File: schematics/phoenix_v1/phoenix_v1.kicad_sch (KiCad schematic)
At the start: 1 part, among them U1 ESP32-DevKitC

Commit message: v1 schematic
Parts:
- removed U1: ESP32-DevKitC, PCM_Espressif:ESP32-DevKitC, symbol PCM_Espressif:ESP32-DevKitC
- added D1, D2, D3: LED, symbol Device:LED
- added L1: L, symbol Device:L
- added R1, R2, R3: R, symbol Device:R
- added R4, R5: 4.7k, symbol Device:R
- added SW2: RotaryEncoder_Switch, symbol Device:RotaryEncoder_Switch
- added U2: MAX31856, Package_SO:TSSOP-14_4.4x5mm_P0.65mm, symbol Sensor_Temperature:MAX31856
- added U3: NHD-C0220BIZ, Display:NHD-C0220BiZ, symbol Display_Character:NHD-C0220BIZ
- added U4: HHG1D-1, Relay_THT:Relay_NCR_HHG1D-1, symbol Relay_SolidState:HHG1D-1
- added U5: ESP32-S3-DevKitC, PCM_Espressif:ESP32-S3-DevKitC, symbol PCM_Espressif:ESP32-S3-DevKitC
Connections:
- new net: R1.1, U5.14 (GPIO46)
- new net: R2.1, U5.28 (GPIO47)
- new net: R3.1, U5.29 (GPIO48)
- new net: D3.2 (A), R3.2
- new net: D1.2 (A), R1.2
- new net: D2.2 (A), R2.2
- new net: L1.1, U4.1
- new net +3.3V: R4.1, R5.1, U5.1 (3V3), U5.2 (3V3)
- new net +5V: U2.5 (AVDD), U2.8 (DVDD), U3.5 (VDD), U5.21 (5V)
- new net AC: L1.2, U4.2
- new net ENC_A: SW2.A, U5.33 (GPIO36)
- new net ENC_B: SW2.B, U5.34 (GPIO37)
- new net ENC_SW: SW2.S2, U5.35 (GPIO38)
- new net GND: D1.1 (K), D2.1 (K), D3.1 (K), SW2.C, SW2.S1, U2.1 (AGND), U2.14 (DGND), U3.4 (VSS), U4.4, U5.22 (GND), U5.23 (GND), U5.24 (GND), U5.44 (GND)
- new net SCL: R4.2, U3.2 (SCL), U5.13 (GPIO3/ADC1_CH2)
- new net SDA: R5.2, U3.3 (SDA), U5.40 (GPIO2/ADC1_CH1)
- new net SSR_PWM: U4.3, U5.27 (GPIO21)
- new net THERMO_CS: U2.9 (~{CS}), U5.16 (GPIO10/ADC1_CH9)
- new net THERMO_SCK: U2.10 (SCK), U5.18 (GPIO12/ADC2_CH1)
- new net THERMO_SDI: U2.12 (SDI), U5.17 (GPIO11/ADC2_CH0)
- new net THERMO_SDO: U2.11 (SDO), U5.19 (GPIO13/ADC2_CH2)
- no-connect marks 0 -> 10

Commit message: screw terminal
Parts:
- added J1: Screw_Terminal_01x02, symbol Connector:Screw_Terminal_01x02
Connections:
- net GND: now also J1.1 (Pin_1)
- net SSR_PWM: now also J1.2 (Pin_2)
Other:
- moved on the sheet: L1, U4

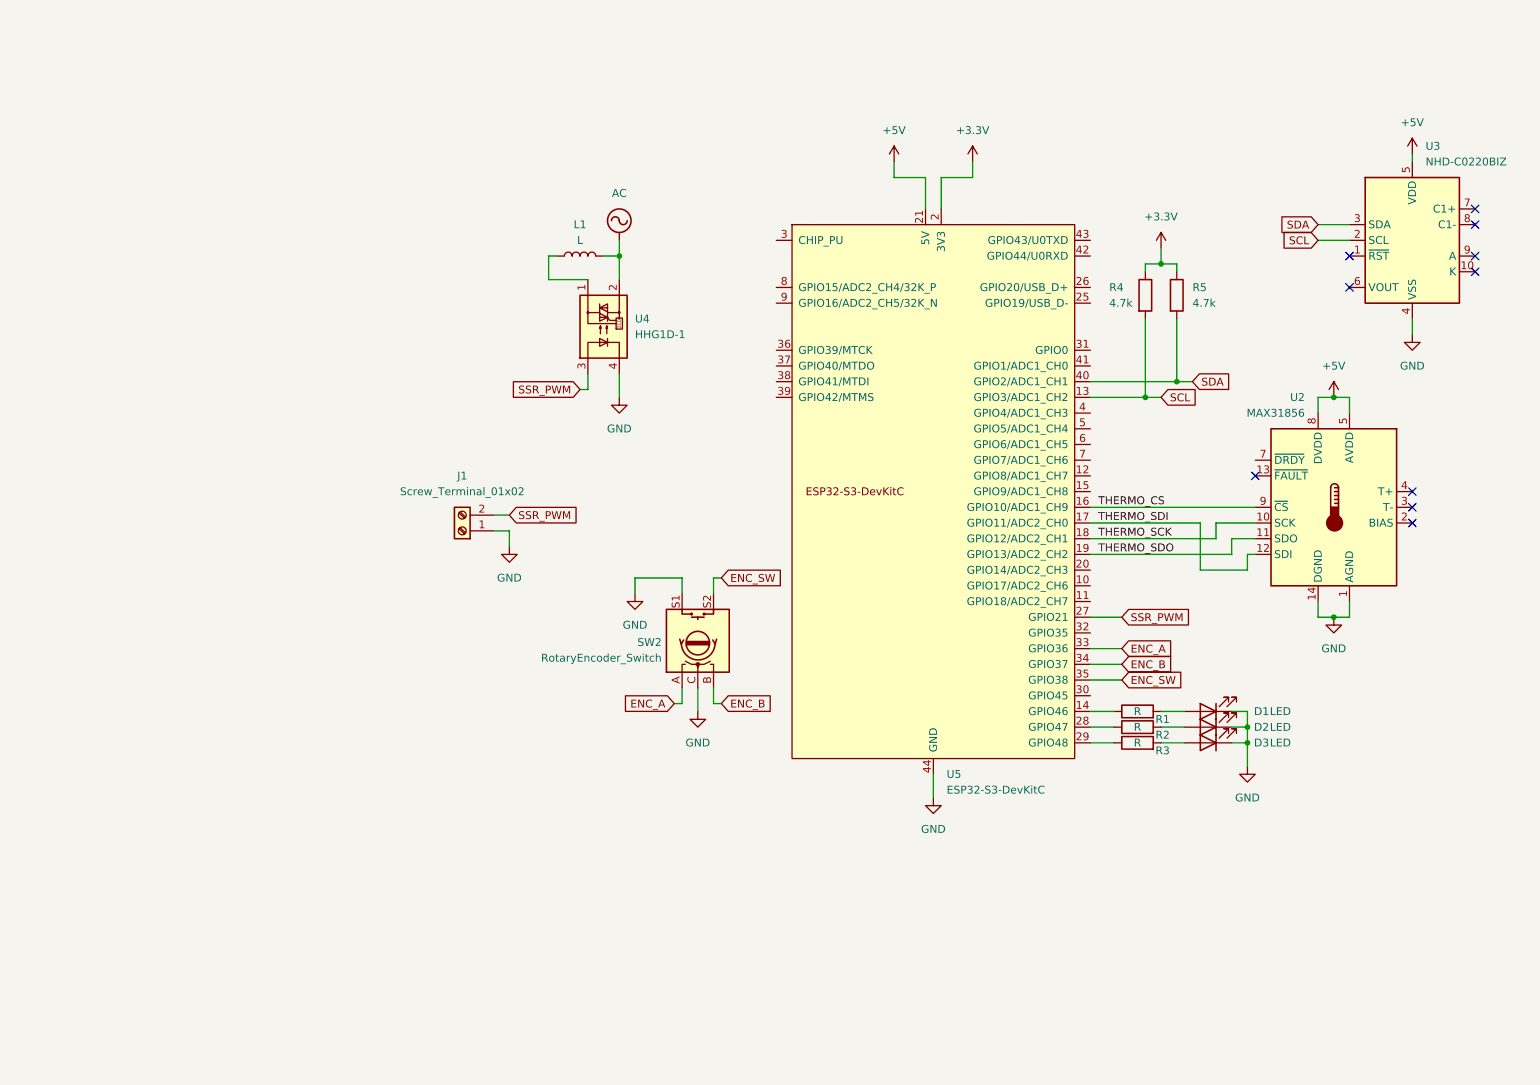
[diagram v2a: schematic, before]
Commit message: assign footprints (#17)
* layout

* fix duplicate

* max31856 socket

* add ncs

* upload screw terminal files

* footprint assignment

* upload MAX31856 eagle-converted source

* create custom footprint for MAX31856 header

* upload pec stuff

* use project footprint library

* extract PEC footprint and sym

* finish assigning footprints and update PCB

---------

Co-authored-by: Waterloo Hacker Fab <waterloofab@hackerfabmacmini.uwaterloo.ca>
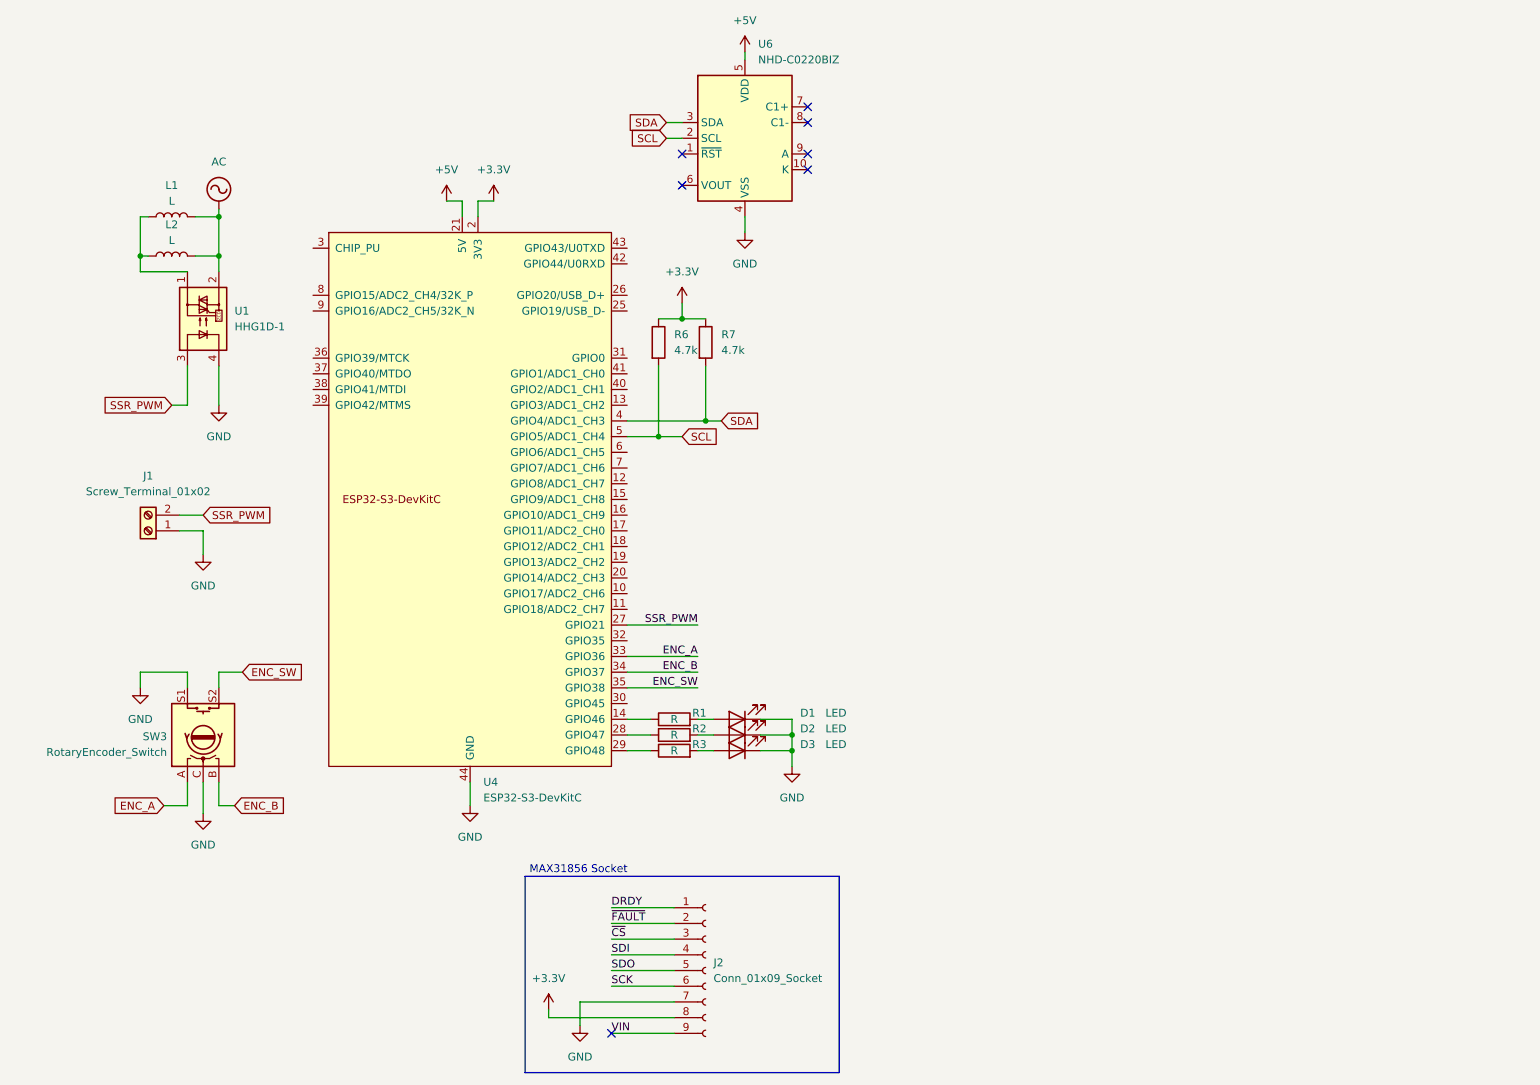
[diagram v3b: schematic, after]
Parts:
- removed R4, R5: 4.7k, symbol Device:R
- removed SW2: RotaryEncoder_Switch, symbol Device:RotaryEncoder_Switch
- removed U2: MAX31856, Package_SO:TSSOP-14_4.4x5mm_P0.65mm, symbol Sensor_Temperature:MAX31856
- removed U3: NHD-C0220BIZ, Display:NHD-C0220BiZ, symbol Display_Character:NHD-C0220BIZ
- removed U4: HHG1D-1, Relay_THT:Relay_NCR_HHG1D-1, symbol Relay_SolidState:HHG1D-1
- removed U5: ESP32-S3-DevKitC, PCM_Espressif:ESP32-S3-DevKitC, symbol PCM_Espressif:ESP32-S3-DevKitC
- added J2: Conn_01x09_Socket, !footprints:MAX31856_HEADER, symbol Connector:Conn_01x09_Socket
- added L2: L, symbol Device:L
- added R6, R7: 4.7k, Resistor_SMD:R_0805_2012Metric_Pad1.20x1.40mm_HandSolder, symbol Device:R
- added SW3: RotaryEncoder_Switch, !footprints:PEC164120FS0012, symbol Device:RotaryEncoder_Switch
- added U1: HHG1D-1, Relay_THT:Relay_NCR_HHG1D-1, symbol Relay_SolidState:HHG1D-1
- added U4: ESP32-S3-DevKitC, PCM_Espressif:ESP32-S3-DevKitC, symbol PCM_Espressif:ESP32-S3-DevKitC
- added U6: NHD-C0220BIZ, Display:NHD-C0220BiZ, symbol Display_Character:NHD-C0220BIZ
- D1, D2, D3: footprint (none) -> Diode_SMD:D_0805_2012Metric_Pad1.15x1.40mm_HandSolder
- J1: footprint (none) -> phoenix_footprints:TE_282837-2
- R1, R2, R3: footprint (none) -> Resistor_SMD:R_0805_2012Metric_Pad1.20x1.40mm_HandSolder
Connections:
- net +3.3V: now also J2.8 (Pin_8), R6.1, R7.1, U4.1 (3V3), U4.2 (3V3)
- net +5V: now also U4.21 (5V), U6.5 (VDD)
- net AC: now also L2.2, U1.2
- net ENC_A: now also SW3.A, U4.33 (GPIO36)
- net ENC_B: now also SW3.B, U4.34 (GPIO37)
- net ENC_SW: now also SW3.S2, U4.35 (GPIO38)
- net GND: now also J2.7 (Pin_7), SW3.C, SW3.S1, U1.4, U4.22 (GND), U4.23 (GND), U4.24 (GND), U4.44 (GND), U6.4 (VSS)
- net SCL: now also R6.2, U4.5 (GPIO5/ADC1_CH4), U6.2 (SCL)
- net SDA: now also R7.2, U4.4 (GPIO4/ADC1_CH3), U6.3 (SDA)
- net SSR_PWM: now also U1.3, U4.27 (GPIO21)
- net at R1.1: now also U4.14 (GPIO46)
- net at R2.1: now also U4.28 (GPIO47)
- net at R3.1: now also U4.29 (GPIO48)
- net at L1.1: now also L2.1, U1.1
- new net DRDY: J2.1 (Pin_1)
- new net SCK: J2.6 (Pin_6)
- new net SDI: J2.4 (Pin_4)
- new net SDO: J2.5 (Pin_5)
- new net VIN: J2.9 (Pin_9)
- new net ~{CS}: J2.3 (Pin_3)
- new net ~{FAULT}: J2.2 (Pin_2)
- no-connect marks 10 -> 7
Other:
- note added: "MAX31856 Socket"

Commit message: exclude relay and inductors from board
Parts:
- U1: footprint Relay_THT:Relay_NCR_HHG1D-1 -> (none)
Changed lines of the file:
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@@
 		(exclude_from_sim no)
 		(in_bom yes)
-		(on_board yes)
+		(on_board no)
 		(dnp no)
 		(fields_autoplaced yes)
@@
 		(exclude_from_sim no)
 		(in_bom yes)
-		(on_board yes)
+		(on_board no)
 		(dnp no)
 		(fields_autoplaced yes)
@@
 			)
 		)
-		(property "Footprint" "Relay_THT:Relay_NCR_HHG1D-1"
+		(property "Footprint" ""
 			(at 55.88 67.31 0)
 			(effects
@@
 		(exclude_from_sim no)
 		(in_bom yes)
-		(on_board yes)
-		(dnp no)
-		(fields_autoplaced yes)
+		(on_board no)
+		(dnp no)
+		(fields_autoplaced yes)

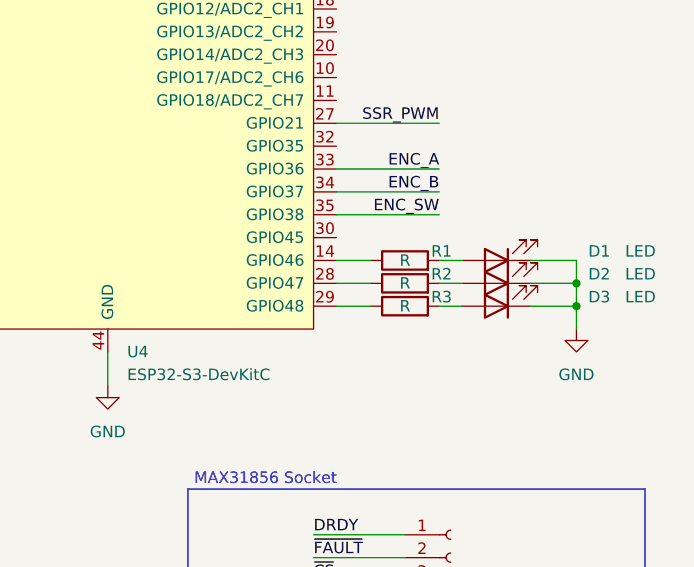
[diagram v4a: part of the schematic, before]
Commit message: set R for leds
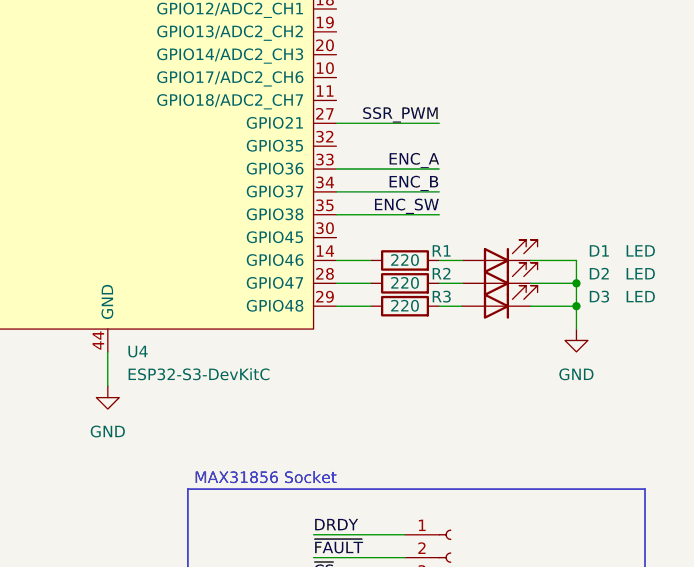
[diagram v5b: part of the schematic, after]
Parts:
- R1, R2, R3: value R -> 220
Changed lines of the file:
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@@
 			)
 		)
-		(property "Value" "R"
+		(property "Value" "220"
 			(at 127 127 90)
 			(effects
@@
 			)
 		)
-		(property "Value" "R"
+		(property "Value" "220"
 			(at 127 129.54 90)
 			(effects
@@
 			)
 		)
-		(property "Value" "R"
+		(property "Value" "220"
 			(at 127 132.08 90)
 			(effects

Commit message: reannotate (#20)
Co-authored-by: Waterloo Hacker Fab <waterloofab@hackerfabmacmini.uwaterloo.ca>
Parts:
- renumbered R6 to R4, R7 to R5, SW3 to SW1, U4 to U2, U6 to U3
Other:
- moved on the sheet: R4, R5, U3

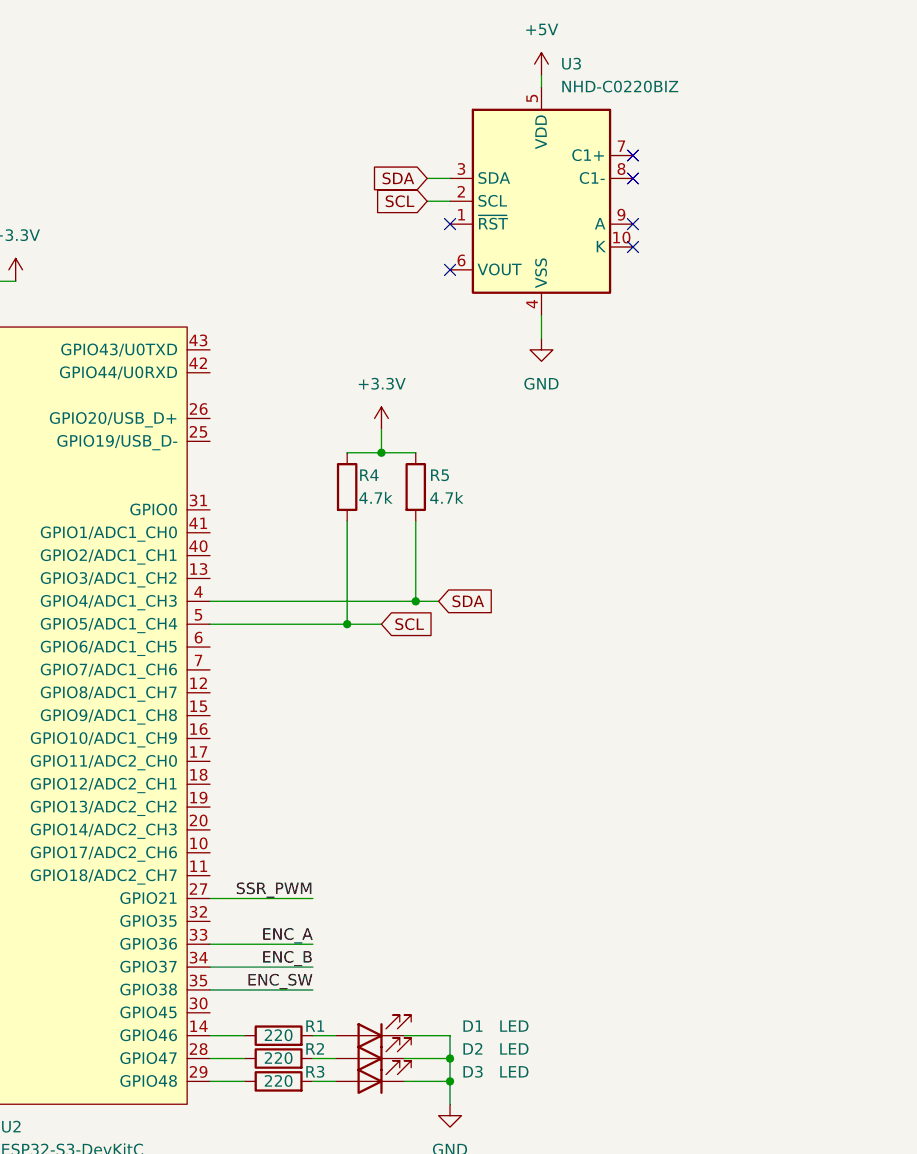
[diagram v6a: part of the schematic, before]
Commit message: caps for display (#21)
Co-authored-by: Waterloo Hacker Fab <waterloofab@hackerfabmacmini.uwaterloo.ca>
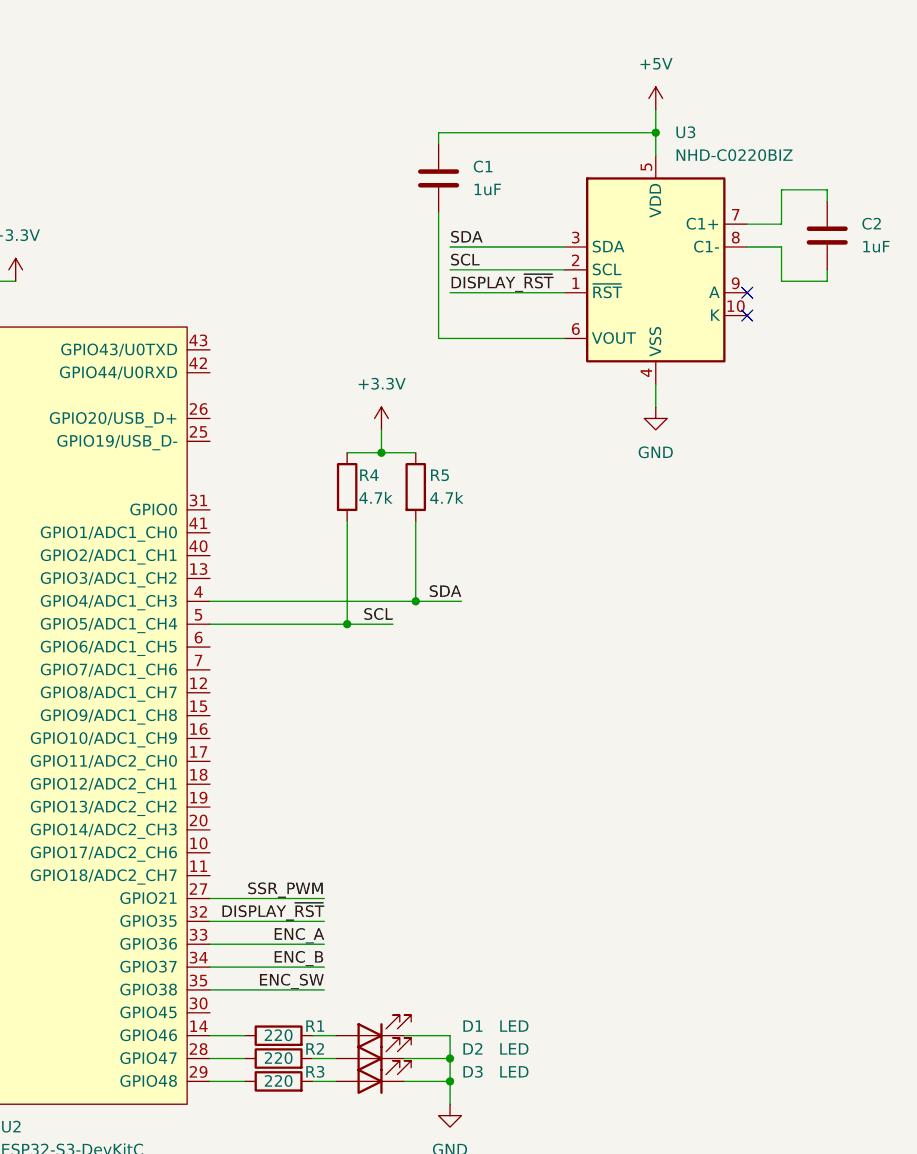
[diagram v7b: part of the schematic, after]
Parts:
- added C1, C2: 1uF, Capacitor_SMD:C_0805_2012Metric, symbol Device:C
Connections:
- net +5V: now also C1.1
- net DISPLAY_~{RST}: now reaches U2.32 (GPIO35)
- net DISPLAY_~{RST}: now also U3.1 (~{RST})
- net at U3.6 (VOUT): now also C1.2
- net at U3.7 (C1+): now also C2.1
- net at U3.8 (C1-): now also C2.2
- no-connect marks 7 -> 3
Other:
- moved on the sheet: U3
